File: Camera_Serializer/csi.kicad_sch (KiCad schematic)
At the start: 0 parts

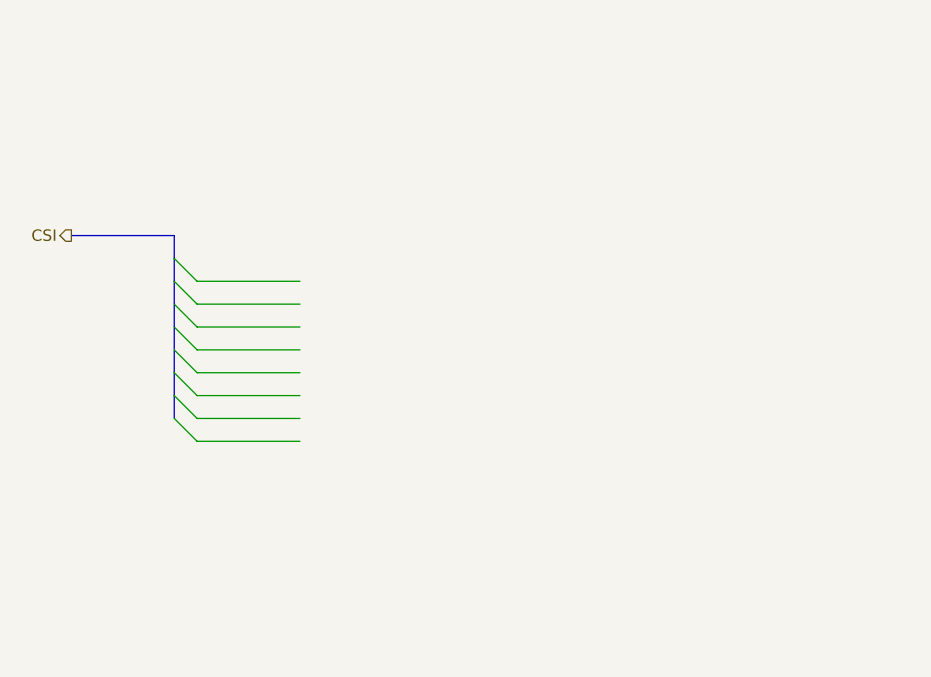
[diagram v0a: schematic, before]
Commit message: Added tvs diodes
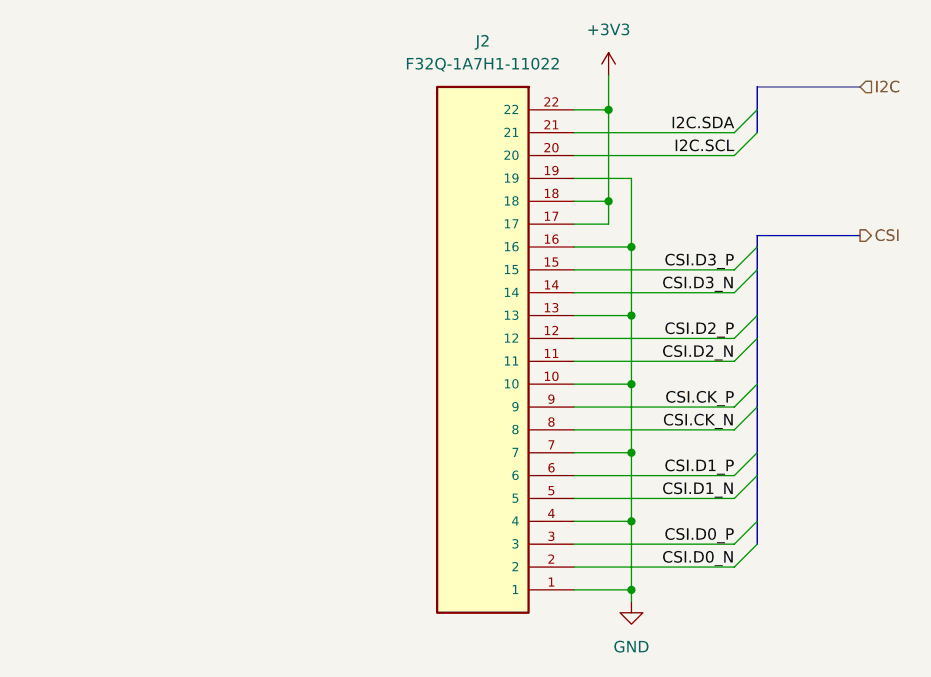
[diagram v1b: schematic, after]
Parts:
- added J2: F32Q-1A7H1-11022, CameraServer_Footprints:F32Q-1A7H1-11022, symbol CameraServer_Symbols:F32Q-1A7H1-11022
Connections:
- new net +3V3: J2.17, J2.18, J2.22
- new net CSI.CK_N: J2.8
- new net CSI.CK_P: J2.9
- new net CSI.D0_N: J2.2
- new net CSI.D0_P: J2.3
- new net CSI.D1_N: J2.5
- new net CSI.D1_P: J2.6
- new net CSI.D2_N: J2.11
- new net CSI.D2_P: J2.12
- new net CSI.D3_N: J2.14
- new net CSI.D3_P: J2.15
- new net GND: J2.1, J2.10, J2.13, J2.16, J2.19, J2.4, J2.7
- new net I2C.SCL: J2.20
- new net I2C.SDA: J2.21

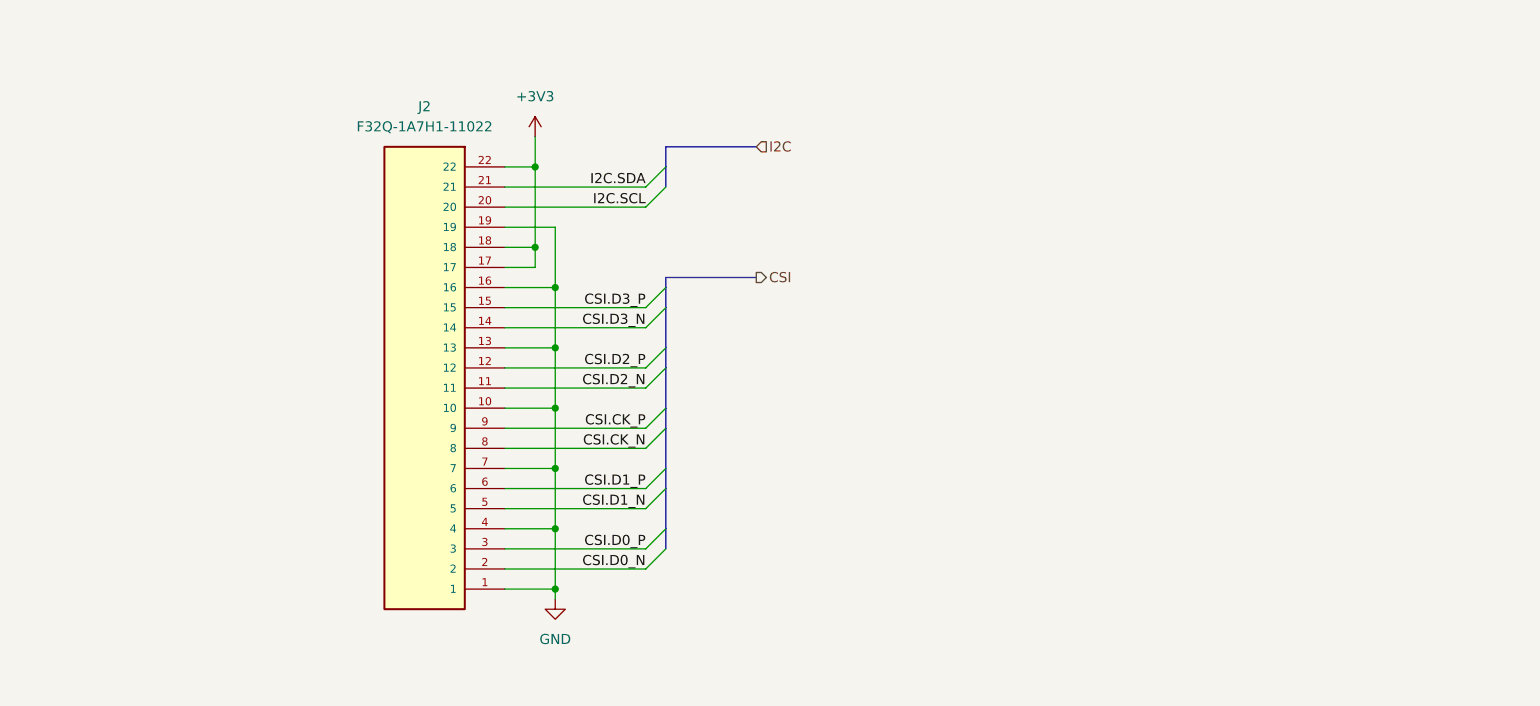
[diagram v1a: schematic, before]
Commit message: Finished CSI interface
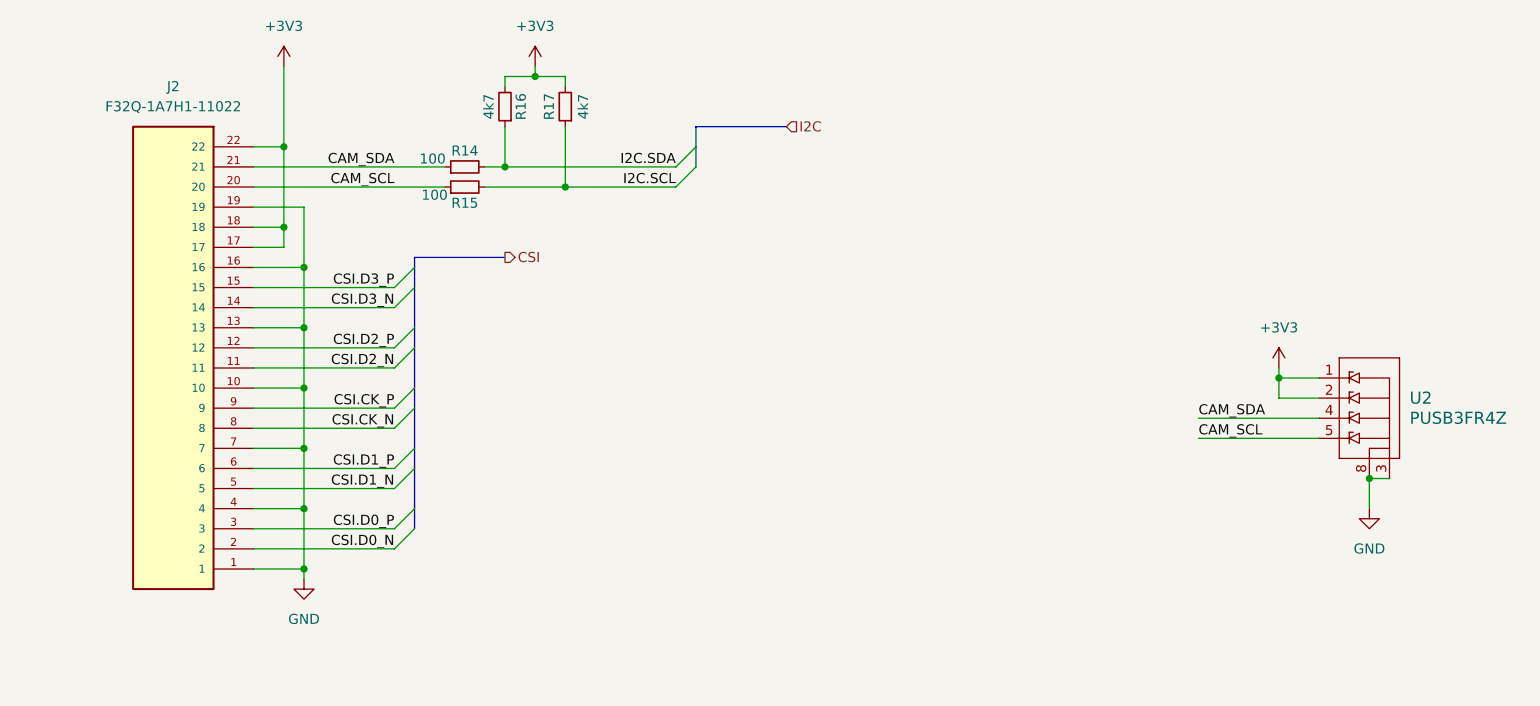
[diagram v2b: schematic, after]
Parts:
- added R14, R15: 100, Resistor_SMD:R_0402_1005Metric_Pad0.72x0.64mm_HandSolder, symbol Device:R_Small
- added R16, R17: 4k7, Resistor_SMD:R_0402_1005Metric_Pad0.72x0.64mm_HandSolder, symbol Device:R_Small
- added U2: PUSB3FR4Z, CameraServer_Footprints:PUSB3FR4Z, symbol CameraServer_Symbols:PUSB3FR4Z
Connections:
- net +3V3: now also R16.2, R17.2, U2.1, U2.2
- net GND: now also U2.3, U2.8
- net I2C.SCL: now also R15.2, R17.1; no longer J2.20
- net I2C.SDA: now also R14.2, R16.1; no longer J2.21
- new net CAM_SCL: J2.20, R15.1, U2.5
- new net CAM_SDA: J2.21, R14.1, U2.4
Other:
- moved on the sheet: J2

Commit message: Finishe schematic
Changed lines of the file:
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@@
 		)
 	)
-	(hierarchical_label "CSI"
+	(hierarchical_label "CSI{CSI}"
 		(shape output)
 		(at 134.62 83.82 0)
@@
 		)
 	)
-	(hierarchical_label "I2C"
+	(hierarchical_label "I2C{I2C}"
 		(shape input)
 		(at 170.18 67.31 0)

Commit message: Switched out 1.2V LDO for better one
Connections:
- net GND: now also J2.SH1, J2.SH2
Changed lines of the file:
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@@
+	)
+	(junction
+		(at 109.22 128.27)
+		(diameter 0)
+		(color 0 0 0 0)
+	)
+	(junction
+		(at 109.22 125.73)
+		(diameter 0)
+		(color 0 0 0 0)
 	)
 	(junction
@@
 	(wire
 		(pts
+			(xy 102.87 125.73) (xy 109.22 125.73)
+		)
+		(stroke
+			(width 0)
+			(type default)
+		)
+	)
+	(wire
+		(pts
 			(xy 106.68 69.85) (xy 106.68 80.01)
 		)
@@
 	(wire
 		(pts
-			(xy 109.22 124.46) (xy 109.22 123.19)
+			(xy 109.22 132.08) (xy 109.22 128.27)
 		)
 		(stroke
@@
 	(wire
 		(pts
+			(xy 109.22 125.73) (xy 109.22 123.19)
+		)
+		(stroke
+			(width 0)
+			(type default)
+		)
+	)
+	(wire
+		(pts
 			(xy 106.68 59.69) (xy 106.68 69.85)
 		)
@@
 		)
 	)
+	(wire
+		(pts
+			(xy 102.87 128.27) (xy 109.22 128.27)
+		)
+		(stroke
+			(width 0)
+			(type default)
+		)
+	)
 	(bus
 		(pts
@@
 		(pts
 			(xy 102.87 100.33) (xy 109.22 100.33)
+		)
+		(stroke
+			(width 0)
+			(type default)
+		)
+	)
+	(wire
+		(pts
+			(xy 109.22 128.27) (xy 109.22 125.73)
 		)
 		(stroke
@@
 	(symbol
 		(lib_id "power:GND")
-		(at 109.22 124.46 0)
+		(at 109.22 132.08 0)
 		(unit 1)
 		(exclude_from_sim no)
@@
 		(fields_autoplaced yes)
 		(property "Reference" "#PWR022"
-			(at 109.22 130.81 0)
+			(at 109.22 138.43 0)
 			(effects
 				(font
@@
 		)
 		(property "Value" "GND"
-			(at 109.22 129.54 0)
+			(at 109.22 137.16 0)
 			(effects
 				(font
@@
 		)
 		(property "Footprint" ""
-			(at 109.22 124.46 0)
+			(at 109.22 132.08 0)
 			(effects
 				(font
@@
 		)
 		(property "Datasheet" ""
-			(at 109.22 124.46 0)
+			(at 109.22 132.08 0)
 			(effects
 				(font
@@
 		)
 		(property "Description" "Power symbol creates a global label with name \"GND\" , ground"
-			(at 109.22 124.46 0)
+			(at 109.22 132.08 0)
 			(effects
 				(font
@@
 		(pin "15"
 		)
+		(pin "SH1"
+		)
+		(pin "SH2"
+		)
 		(instances

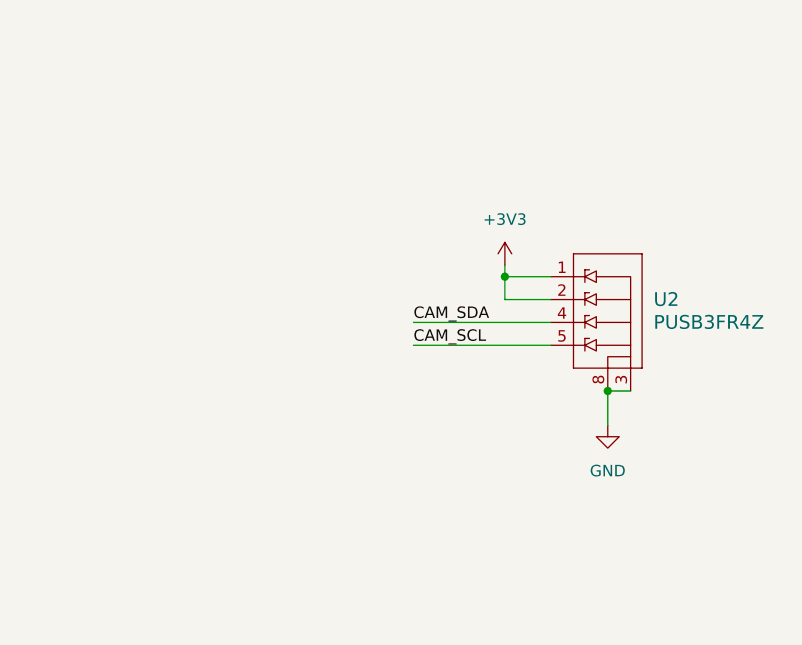
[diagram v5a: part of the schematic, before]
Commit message: All components placed in correct positions
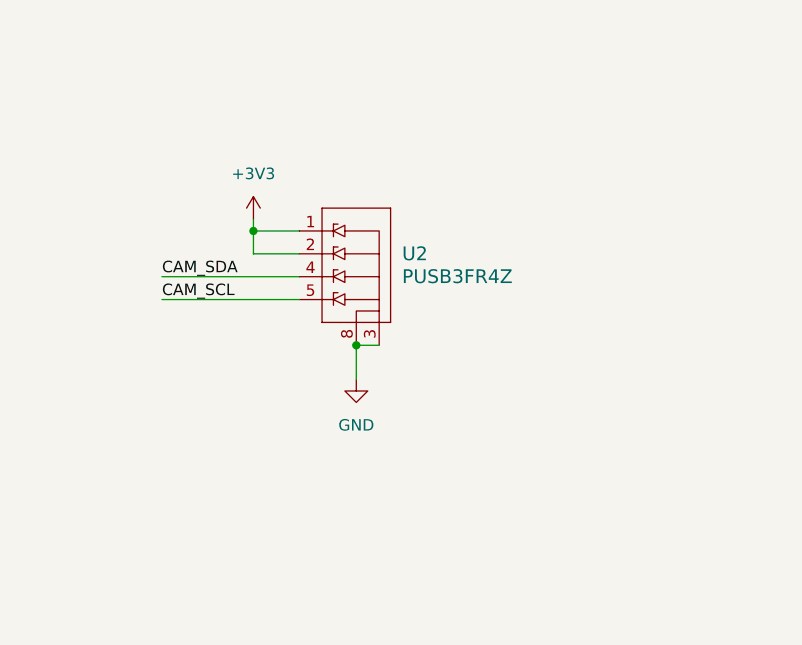
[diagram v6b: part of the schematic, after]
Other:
- moved on the sheet: U2
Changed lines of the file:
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@@
 	)
 	(junction
-		(at 243.84 111.76)
+		(at 215.9 106.68)
 		(diameter 0)
 		(color 0 0 0 0)
@@
 	)
 	(junction
-		(at 232.41 99.06)
+		(at 204.47 93.98)
 		(diameter 0)
 		(color 0 0 0 0)
@@
 	(wire
 		(pts
-			(xy 232.41 99.06) (xy 237.49 99.06)
+			(xy 204.47 93.98) (xy 209.55 93.98)
 		)
 		(stroke
@@
 	(wire
 		(pts
-			(xy 243.84 111.76) (xy 246.38 111.76)
+			(xy 215.9 106.68) (xy 218.44 106.68)
 		)
 		(stroke
@@
 	(wire
 		(pts
-			(xy 222.25 104.14) (xy 237.49 104.14)
+			(xy 194.31 99.06) (xy 209.55 99.06)
 		)
 		(stroke
@@
 	(wire
 		(pts
-			(xy 243.84 111.76) (xy 243.84 115.57)
+			(xy 215.9 106.68) (xy 215.9 110.49)
 		)
 		(stroke
@@
 	(wire
 		(pts
-			(xy 222.25 106.68) (xy 237.49 106.68)
+			(xy 194.31 101.6) (xy 209.55 101.6)
 		)
 		(stroke
@@
 	(wire
 		(pts
-			(xy 232.41 97.79) (xy 232.41 99.06)
+			(xy 204.47 92.71) (xy 204.47 93.98)
 		)
 		(stroke
@@
 	(wire
 		(pts
-			(xy 237.49 101.6) (xy 232.41 101.6)
+			(xy 209.55 96.52) (xy 204.47 96.52)
 		)
 		(stroke
@@
 	(wire
 		(pts
-			(xy 232.41 101.6) (xy 232.41 99.06)
+			(xy 204.47 96.52) (xy 204.47 93.98)
 		)
 		(stroke
@@
 	)
 	(label "CAM_SDA"
-		(at 222.25 104.14 0)
+		(at 194.31 99.06 0)
 		(fields_autoplaced yes)
 		(effects
@@
 	)
 	(label "CAM_SCL"
-		(at 222.25 106.68 0)
+		(at 194.31 101.6 0)
 		(fields_autoplaced yes)
 		(effects
@@
 	(symbol
 		(lib_id "CameraServer_Symbols:PUSB3FR4Z")
-		(at 243.84 102.87 0)
+		(at 215.9 97.79 0)
 		(unit 1)
 		(exclude_from_sim no)
@@
 		(fields_autoplaced yes)
 		(property "Reference" "U2"
-			(at 248.92 101.5999 0)
+			(at 220.98 96.5199 0)
 			(effects
 				(font
@@
 		)
 		(property "Value" "PUSB3FR4Z"
-			(at 248.92 104.1399 0)
+			(at 220.98 99.0599 0)
 			(effects
 				(font
@@
 		)
 		(property "Footprint" "CameraServer_Footprints:PUSB3FR4Z"
-			(at 256.794 103.632 0)
+			(at 228.854 98.552 0)
 			(effects
 				(font
@@
 		)
 		(property "Datasheet" "PUSB3FR4Z"
-			(at 256.286 101.346 0)
+			(at 228.346 96.266 0)
 			(effects
 				(font
@@
 		)
 		(property "Description" ""
-			(at 232.41 99.06 0)
+			(at 204.47 93.98 0)
 			(effects
 				(font
@@
 	(symbol
 		(lib_id "power:+3V3")
-		(at 232.41 97.79 0)
+		(at 204.47 92.71 0)
 		(unit 1)
 		(exclude_from_sim no)
@@
 		(fields_autoplaced yes)
 		(property "Reference" "#PWR025"
-			(at 232.41 101.6 0)
+			(at 204.47 96.52 0)
 			(effects
 				(font
@@
 		)
 		(property "Value" "+3V3"
-			(at 232.41 92.71 0)
+			(at 204.47 87.63 0)
 			(effects
 				(font
@@
 		)
 		(property "Footprint" ""
-			(at 232.41 97.79 0)
+			(at 204.47 92.71 0)
 			(effects
 				(font
@@
 		)
 		(property "Datasheet" ""
-			(at 232.41 97.79 0)
+			(at 204.47 92.71 0)
 			(effects
 				(font
@@
 		)
 		(property "Description" "Power symbol creates a global label with name \"+3V3\""
-			(at 232.41 97.79 0)
+			(at 204.47 92.71 0)
 			(effects
 				(font
@@
 	(symbol
 		(lib_id "power:GND")
-		(at 243.84 115.57 0)
+		(at 215.9 110.49 0)
 		(unit 1)
 		(exclude_from_sim no)
@@
 		(fields_autoplaced yes)
 		(property "Reference" "#PWR024"
-			(at 243.84 121.92 0)
+			(at 215.9 116.84 0)
 			(effects
 				(font
@@
 		)
 		(property "Value" "GND"
-			(at 243.84 120.65 0)
+			(at 215.9 115.57 0)
 			(effects
 				(font
@@
 		)
 		(property "Footprint" ""
-			(at 243.84 115.57 0)
+			(at 215.9 110.49 0)
 			(effects
 				(font
@@
 		)
 		(property "Datasheet" ""
-			(at 243.84 115.57 0)
+			(at 215.9 110.49 0)
 			(effects
 				(font
@@
 		)
 		(property "Description" "Power symbol creates a global label with name \"GND\" , ground"
-			(at 243.84 115.57 0)
-			(effects
-				(font
+			(at 215.9 110.49 0)
+			(effects
+				(font
